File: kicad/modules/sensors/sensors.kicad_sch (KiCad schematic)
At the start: 52 parts, among them J1 Bus_PCI_Express_x1, J4 Conn_01x02, J6 USB_C_Receptacle_USB2.0_16P, U2 RP2040, U4 W25Q128JVP, U5 BMP388, U8 BNO055, U9 MCP25625T-E/ML, X1 ABM8-272-T3, Y1 ABS07-32.768KHZ-T, Y2 X322516MLB4SI

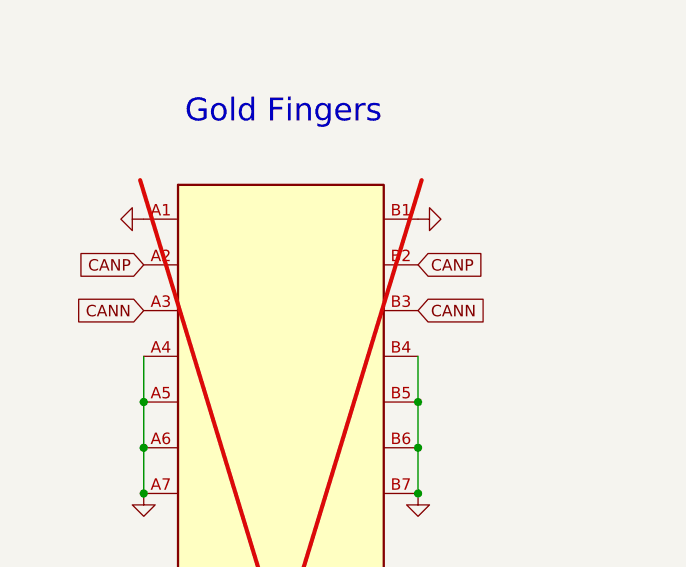
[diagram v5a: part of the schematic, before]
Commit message: sensors: update PCIe pin nets, refine routing
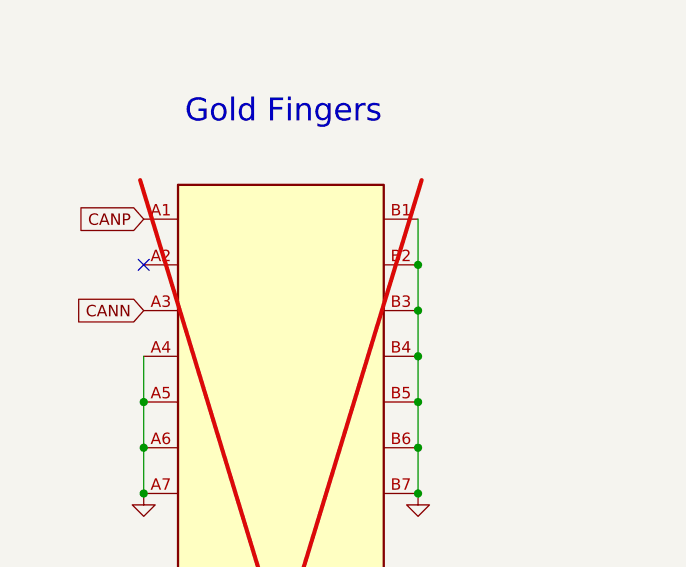
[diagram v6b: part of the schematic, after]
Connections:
- net CANN: no longer J1.B3 (+12V)
- net CANP: now also J1.A1 (~{PRSNT1}); no longer J1.A2 (+12V), J1.B2 (+12V)
- net GND: now also J1.B2 (+12V), J1.B3 (+12V); no longer J1.A1 (~{PRSNT1})
- no-connect marks 30 -> 31
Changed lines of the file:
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@@
 	)
 	(junction
+		(at 91.44 285.75)
+		(diameter 0)
+		(color 0 0 0 0)
+	)
+	(junction
 		(at 60.96 321.31)
 		(diameter 0)
@@
 	)
 	(junction
+		(at 91.44 280.67)
+		(diameter 0)
+		(color 0 0 0 0)
+	)
+	(junction
 		(at 135.89 143.51)
 		(diameter 0)
@@
 	)
 	(junction
+		(at 91.44 275.59)
+		(diameter 0)
+		(color 0 0 0 0)
+	)
+	(junction
 		(at 307.34 135.89)
 		(diameter 0)
@@
 	)
 	(no_connect
+		(at 60.96 275.59)
+	)
+	(no_connect
 		(at 325.12 199.39)
 	)
@@
 	(wire
 		(pts
+			(xy 91.44 280.67) (xy 91.44 285.75)
+		)
+		(stroke
+			(width 0)
+			(type default)
+		)
+	)
+	(wire
+		(pts
 			(xy 387.35 111.76) (xy 387.35 114.3)
 		)
@@
 	(wire
 		(pts
+			(xy 91.44 285.75) (xy 91.44 290.83)
+		)
+		(stroke
+			(width 0)
+			(type default)
+		)
+	)
+	(wire
+		(pts
 			(xy 55.88 321.31) (xy 60.96 321.31)
 		)
@@
 	(wire
 		(pts
-			(xy 91.44 285.75) (xy 91.44 290.83)
-		)
-		(stroke
-			(width 0)
-			(type default)
-		)
-	)
-	(wire
-		(pts
 			(xy 485.14 119.38) (xy 485.14 109.22)
 		)
@@
 	(wire
 		(pts
+			(xy 91.44 270.51) (xy 91.44 275.59)
+		)
+		(stroke
+			(width 0)
+			(type default)
+		)
+	)
+	(wire
+		(pts
 			(xy 370.84 347.98) (xy 379.73 347.98)
 		)
@@
 	(wire
 		(pts
+			(xy 91.44 275.59) (xy 91.44 280.67)
+		)
+		(stroke
+			(width 0)
+			(type default)
+		)
+	)
+	(wire
+		(pts
 			(xy 347.98 347.98) (xy 356.87 347.98)
 		)
@@
 		)
 	)
-	(global_label "CANP"
-		(shape input)
-		(at 91.44 275.59 0)
-		(fields_autoplaced yes)
-		(effects
-			(font
-				(size 1.27 1.27)
-			)
-			(justify left)
-		)
-		(property "Intersheetrefs" "${INTERSHEET_REFS}"
-			(at 99.3843 275.59 0)
-			(effects
-				(font
-					(size 1.27 1.27)
-				)
-				(justify left)
-				(hide yes)
-			)
-		)
-	)
 	(global_label "USB_D+"
 		(shape input)
@@
 		)
 	)
-	(global_label "CANN"
-		(shape input)
-		(at 91.44 280.67 0)
-		(fields_autoplaced yes)
-		(effects
-			(font
-				(size 1.27 1.27)
-			)
-			(justify left)
-		)
-		(property "Intersheetrefs" "${INTERSHEET_REFS}"
-			(at 99.4448 280.67 0)
-			(effects
-				(font
-					(size 1.27 1.27)
-				)
-				(justify left)
-				(hide yes)
-			)
-		)
-	)
 	(global_label "BMPINT"
 		(shape input)
@@
 	(global_label "CANP"
 		(shape input)
-		(at 60.96 275.59 180)
+		(at 60.96 270.51 180)
 		(fields_autoplaced yes)
 		(effects
@@
 		)
 		(property "Intersheetrefs" "${INTERSHEET_REFS}"
-			(at 53.0157 275.59 0)
+			(at 53.0157 270.51 0)
 			(effects
 				(font
@@
 					(unit 1)
 				)
-			)
-		)
-	)
-	(symbol
-		(lib_id "power:GND")
-		(at 60.96 270.51 270)
-		(unit 1)
-		(exclude_from_sim no)
-		(in_bom yes)
-		(on_board yes)
-		(dnp no)
-		(fields_autoplaced yes)
-		(property "Reference" "#PWR02"
-			(at 54.61 270.51 0)
-			(effects
-				(font
-					(size 1.27 1.27)
-				)
-				(hide yes)
-			)
-		)
-		(property "Value" "GND"
-			(at 57.15 270.5099 90)
-			(effects
-				(font
-					(size 1.27 1.27)
-				)
-				(justify right)
-				(hide yes)
-			)
-		)
-		(property "Footprint" ""
-			(at 60.96 270.51 0)
-			(effects
-				(font
-					(size 1.27 1.27)
-				)
-				(hide yes)
-			)
-		)
-		(property "Datasheet" ""
-			(at 60.96 270.51 0)
-			(effects
-				(font
-					(size 1.27 1.27)
-				)
-				(hide yes)
-			)
-		)
-		(property "Description" "Power symbol creates a global label with name \"GND\" , ground"
-			(at 60.96 270.51 0)
-			(effects
-				(font
-					(size 1.27 1.27)
-				)
-				(hide yes)
-			)
-		)
-		(pin "1"
-		)
-		(instances
-			(project "sensors"
-				(path "/612ece3f-e722-4b33-8111-645d24cfcf05"
-					(reference "#PWR02")
-					(unit 1)
-				)
-			)
-		)
-	)
-	(symbol
-		(lib_id "power:GND")
-		(at 91.44 270.51 90)
-		(unit 1)
-		(exclude_from_sim no)
-		(in_bom yes)
-		(on_board yes)
-		(dnp no)
-		(fields_autoplaced yes)
-		(property "Reference" "#PWR01"
-			(at 97.79 270.51 0)
-			(effects
-				(font
-					(size 1.27 1.27)
-				)
-				(hide yes)
-			)
-		)
-		(property "Value" "GND"
-			(at 95.25 270.5099 90)
-			(effects
-				(font
-					(size 1.27 1.27)
-				)
-				(justify right)
-				(hide yes)
-			)
-		)
-		(property "Footprint" ""
-			(at 91.44 270.51 0)
-			(effects
-				(font
-					(size 1.27 1.27)
-				)
-				(hide yes)
-			)
-		)
-		(property "Datasheet" ""
-			(at 91.44 270.51 0)
-			(effects
-				(font
-					(size 1.27 1.27)
-				)
-				(hide yes)
-			)
-		)
-		(property "Description" "Power symbol creates a global label with name \"GND\" , ground"
-			(at 91.44 270.51 0)
-			(effects
-				(font
-					(size 1.27 1.27)
-				)
-				(hide yes)
-			)
-		)
-		(pin "1"
-		)
-		(instances
-			(project "sensors"
-				(path "/612ece3f-e722-4b33-8111-645d24cfcf05"
-					(reference "#PWR01")
-					(unit 1)
-				)
